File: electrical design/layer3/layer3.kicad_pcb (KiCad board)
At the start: 2 copper layers, 140 x 140 mm, 61 parts, among them J1 XT60PW-M, J10 SH1.0 Female, J11 SH1.0 Female, J12 MOTOR1, J13 MOTOR2, J14 MOTOR3, J15 MOTOR4, J16 CAMERA, J17 SH1.0 3P, J18 XT30UPB-F, J19 Conn_01x01_Female, J2 XT60PW-M, J20 Conn_01x01_Female, J3 XT30UPB-F, J4 XT30UPB-F, J5 XT30UPB-F, J6 XT30UPB-F, J7 XT30UPB-F, J8 COMPASS, J9 SH1.0 5P, SW1 SW_DPDT_x2, SW2 SW_Push, SW3 SW_DPDT_x2, SW4 SW_Push, U1 TEENSY 4.0, U2 STM32F103C8T6, U3 STM32F103C8T6, U4 74LVC2G04, U5 74LVC2G04, Y1 Crystal, Y2 Crystal

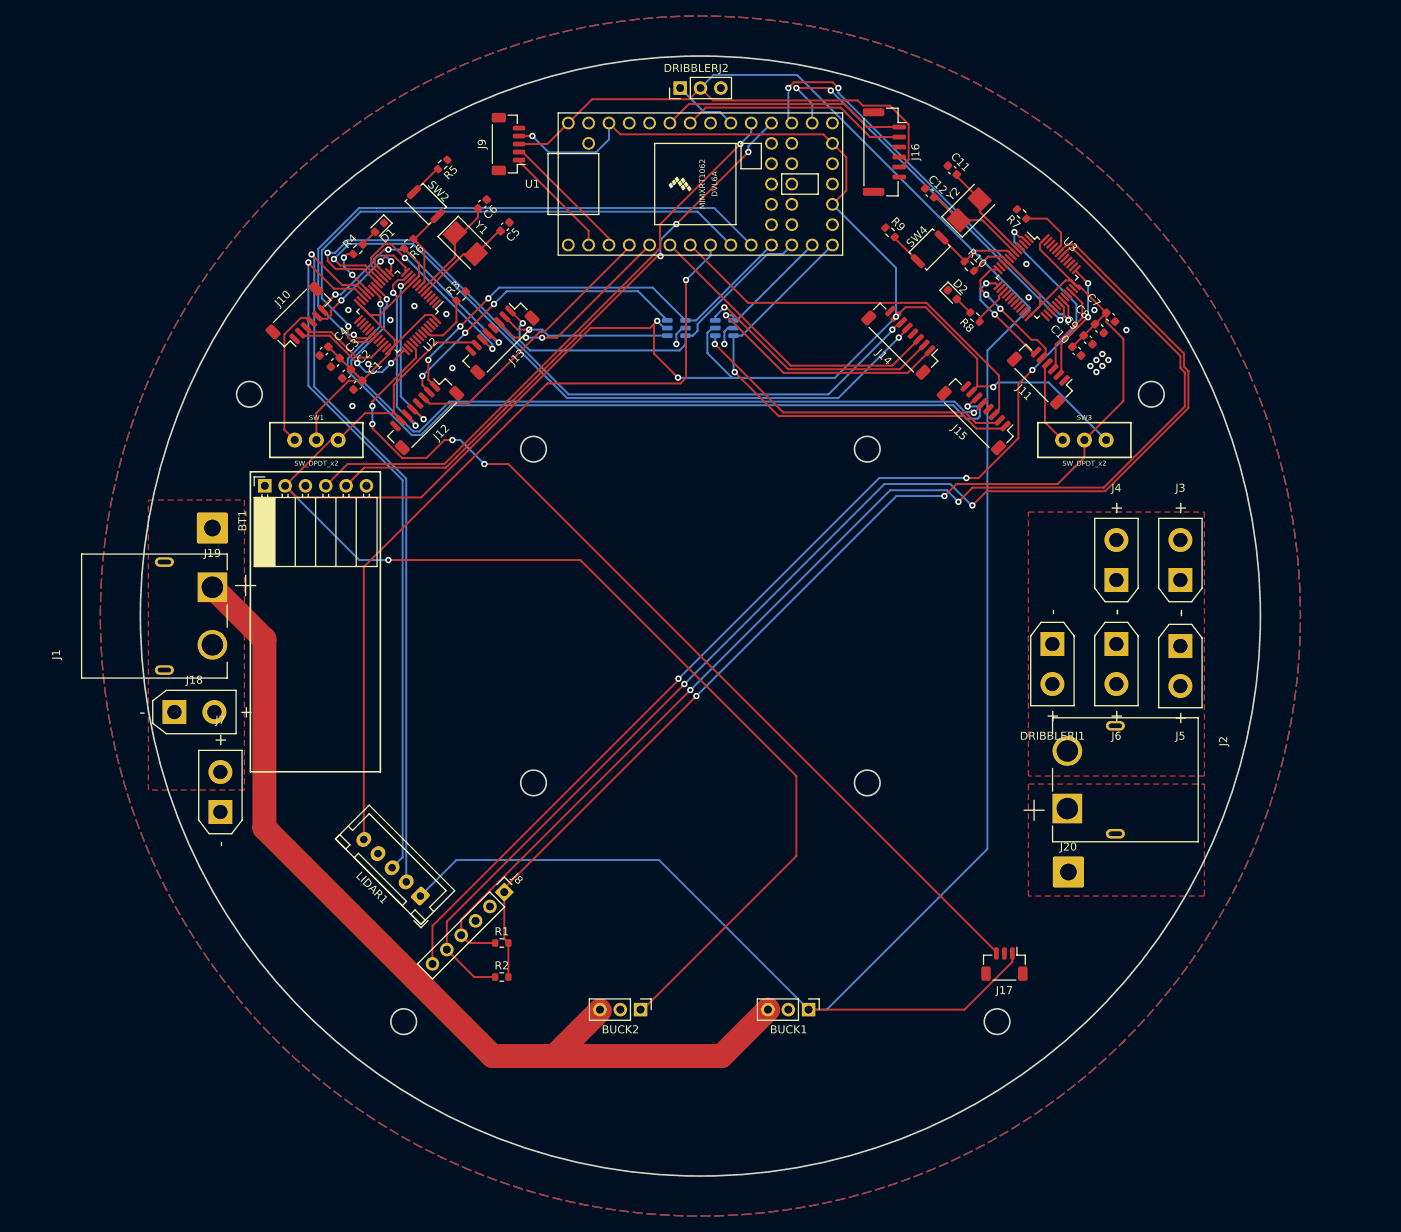
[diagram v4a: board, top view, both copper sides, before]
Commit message: fillet pcb traces
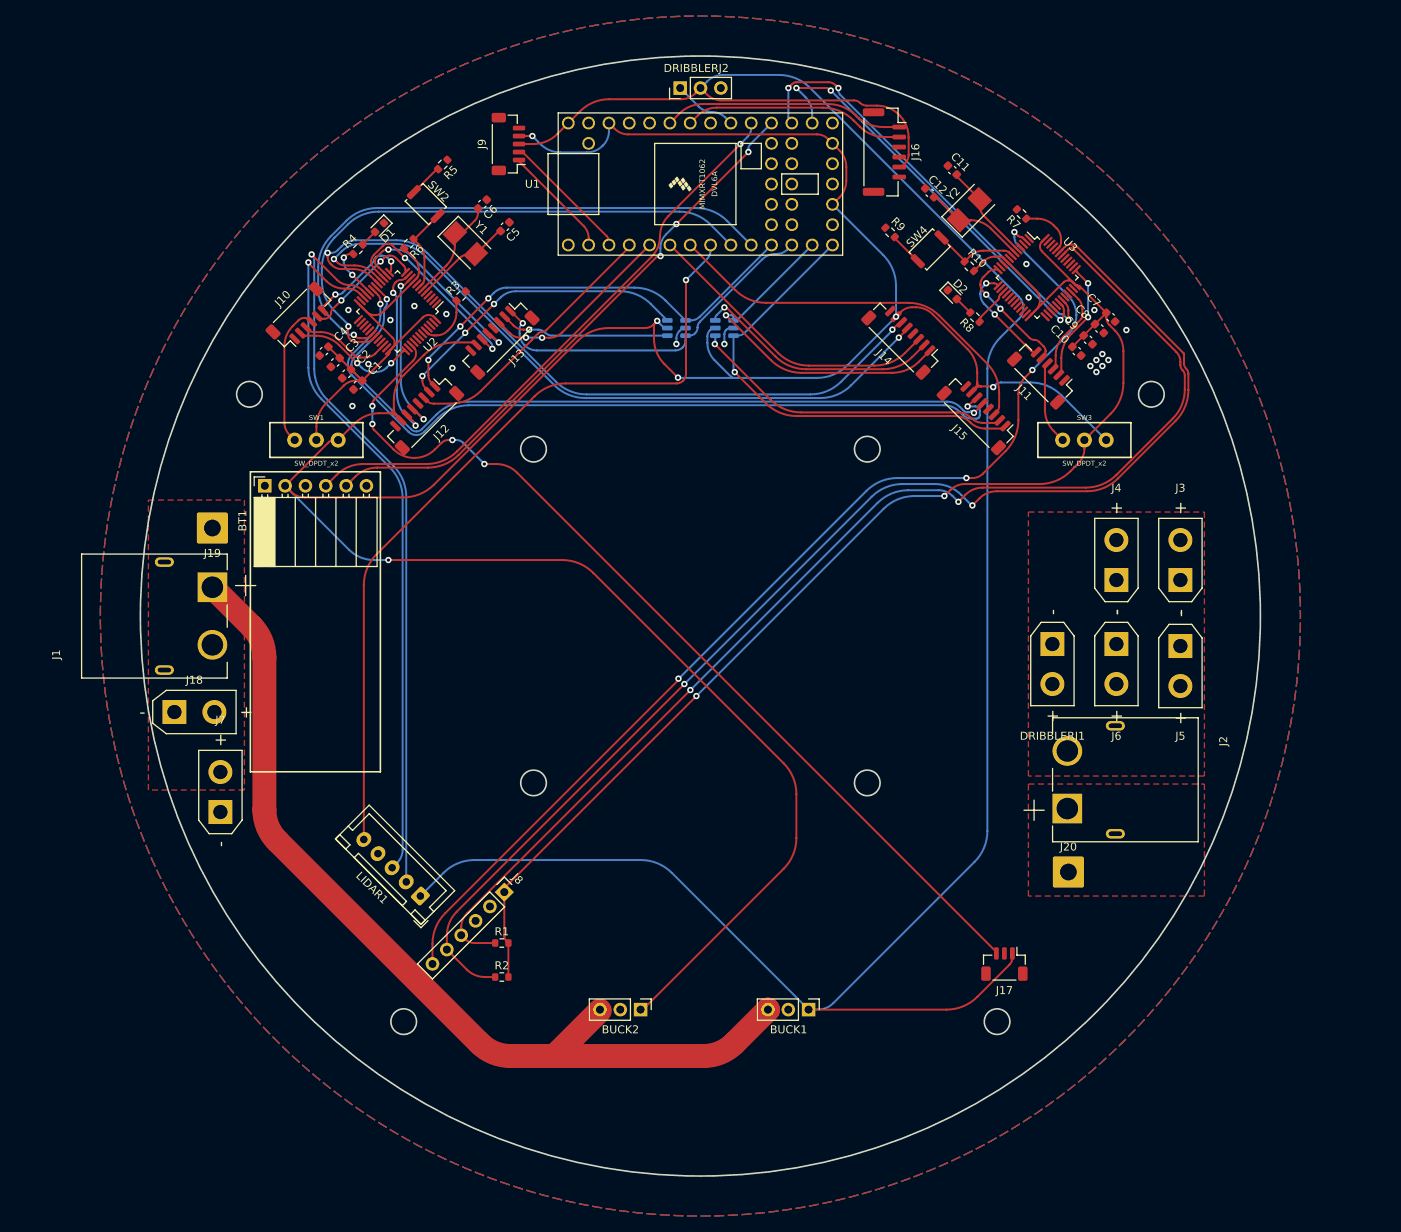
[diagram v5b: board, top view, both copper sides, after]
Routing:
- net +5V: track 301.0 -> 296.9 mm
- net +3V3: track 363.7 -> 361.5 mm
- net /IMUSDA: track 161.2 -> 159.5 mm
- net /MCU3V32: track 168.6 -> 166.9 mm
- net /IMUSCL: track 152.2 -> 150.6 mm
- net /IMURST: track 137.3 -> 135.8 mm
- net /M3C2: track 92.7 -> 91.4 mm
- net /L4RX: track 71.1 -> 69.8 mm
- net /L4TX: track 74.0 -> 72.8 mm
- net /M3C1: track 91.2 -> 90.0 mm
- net /M4C2: track 101.2 -> 100.1 mm
- net /M4C1: track 97.8 -> 96.8 mm
- net /BTTX: track 74.5 -> 73.6 mm
- net /LIDARRX: track 89.9 -> 89.0 mm
- net /M4PWM: track 50.5 -> 49.7 mm
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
